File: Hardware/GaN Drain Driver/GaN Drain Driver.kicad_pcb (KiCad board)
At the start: 4 copper layers, 101.6 x 50.8 mm, 64 parts, among them J1 SMA-J-P-H-ST-EM1, J2 Conn_01x02_Socket, J3 Conn_01x02_Socket, J4 Conn_01x02_Socket, Q1 NVD360N65S3T4G, Q2 NVD360N65S3T4G, U1 IRS2008S, U2 LM393, U3 L7815, U4 R1SE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

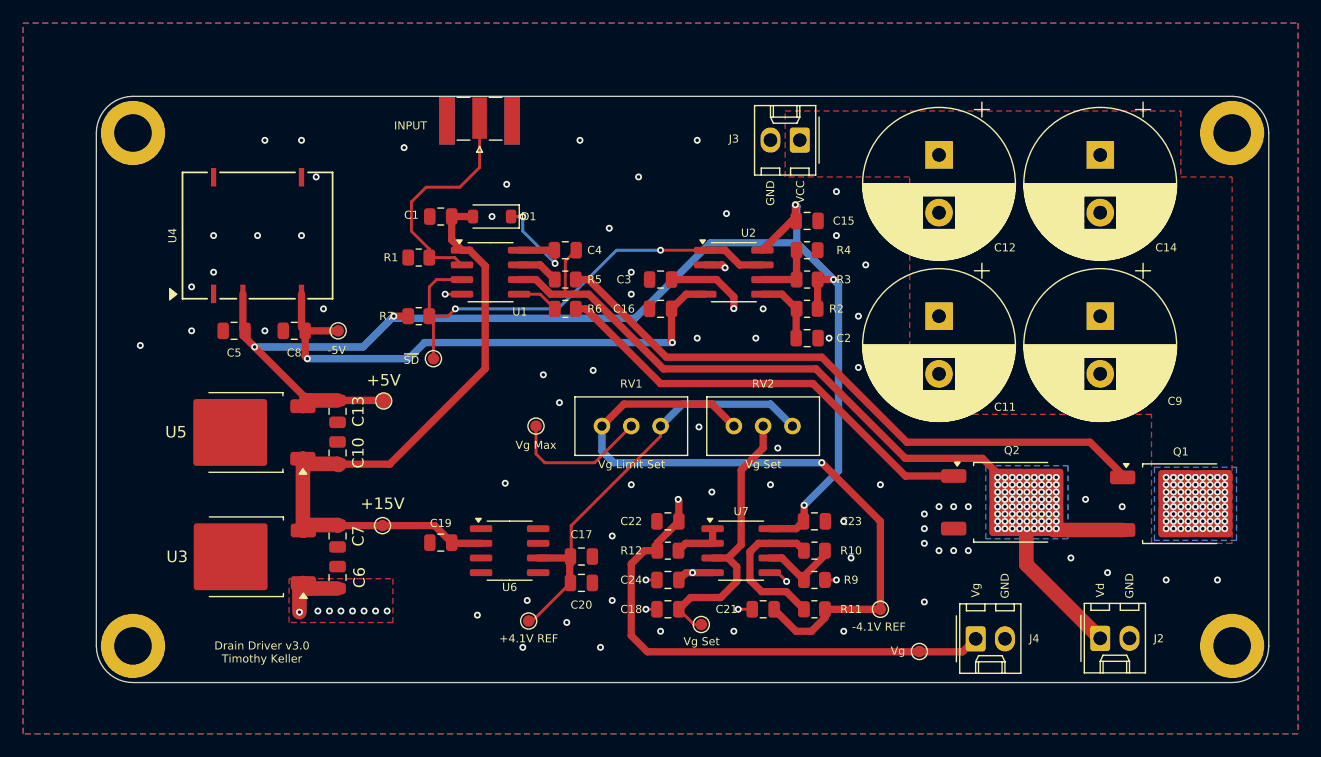
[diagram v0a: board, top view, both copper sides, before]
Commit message: Adding BOM, Fixing schematic issue
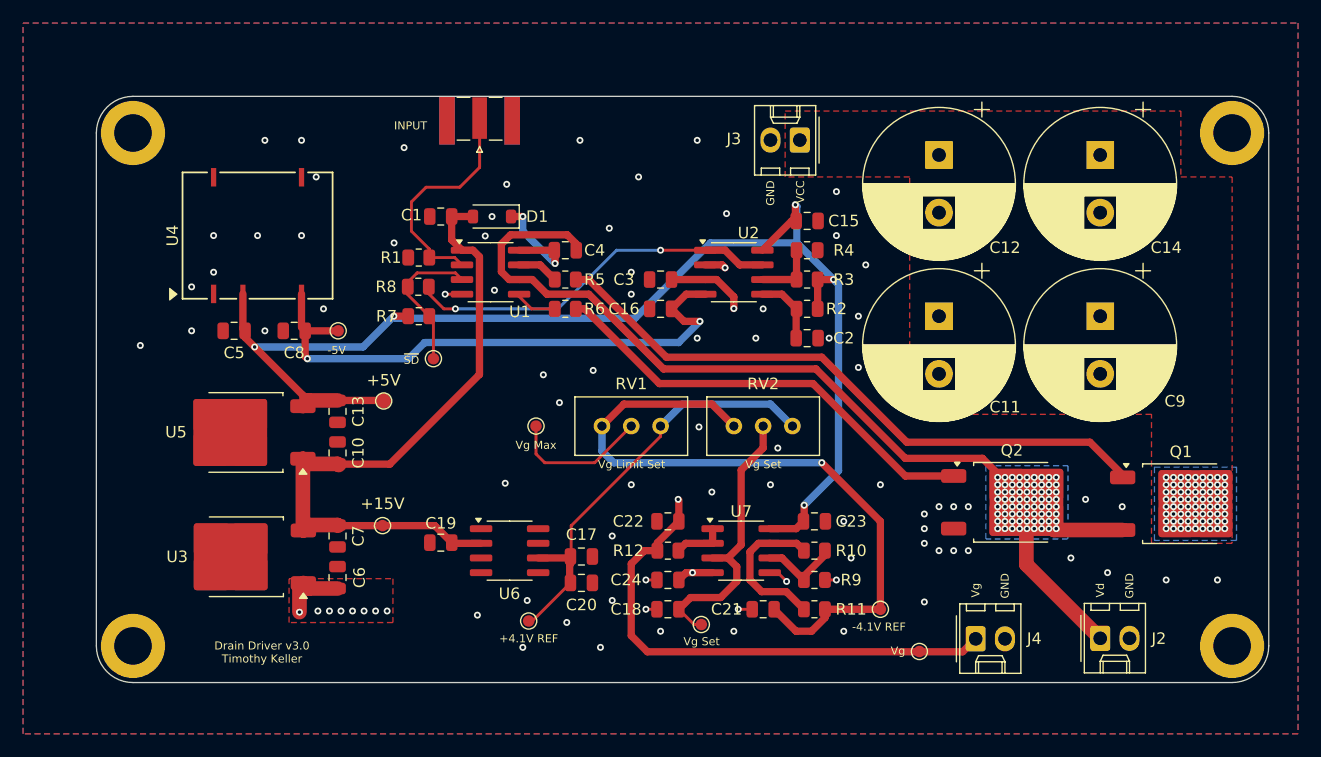
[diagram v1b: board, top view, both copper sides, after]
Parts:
- added R8: 10k, Resistor_SMD:R_0805_2012Metric, F.Cu at (78.7, 41.9)
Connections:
- R7 pad 2: COMP_OUT -> ~{SD}
- TP2 pad 1: COMP_OUT -> ~{SD}
- U1 pad 3: COMP_OUT -> ~{SD}
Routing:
- net ~{SD}: track 0.00 -> 12.8 mm
- net COMP_OUT: track 41.2 -> 32.7 mm
- net Vd: track 80.5 -> 88.2 mm
- net -5V: track 91.5 -> 94.6 mm
- net GND: vias 74 -> 77

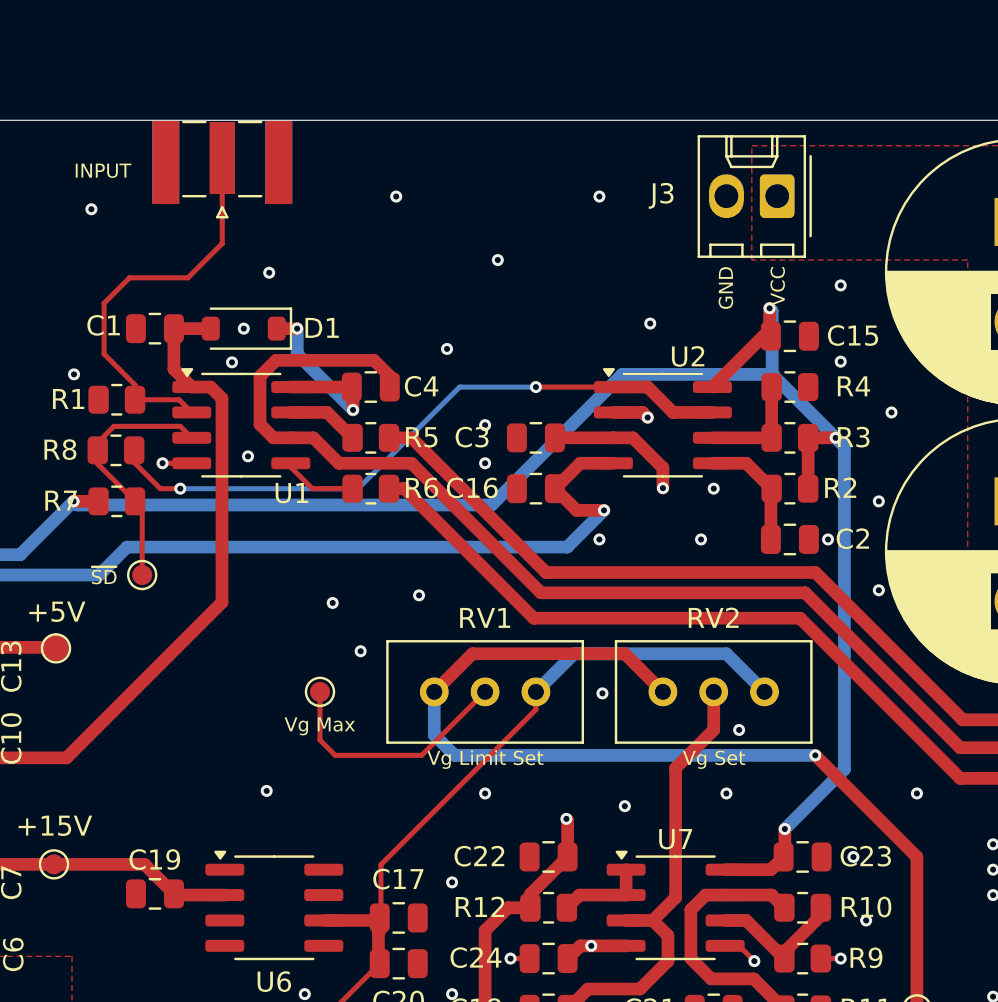
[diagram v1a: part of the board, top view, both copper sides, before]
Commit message: Updating SMA footprint
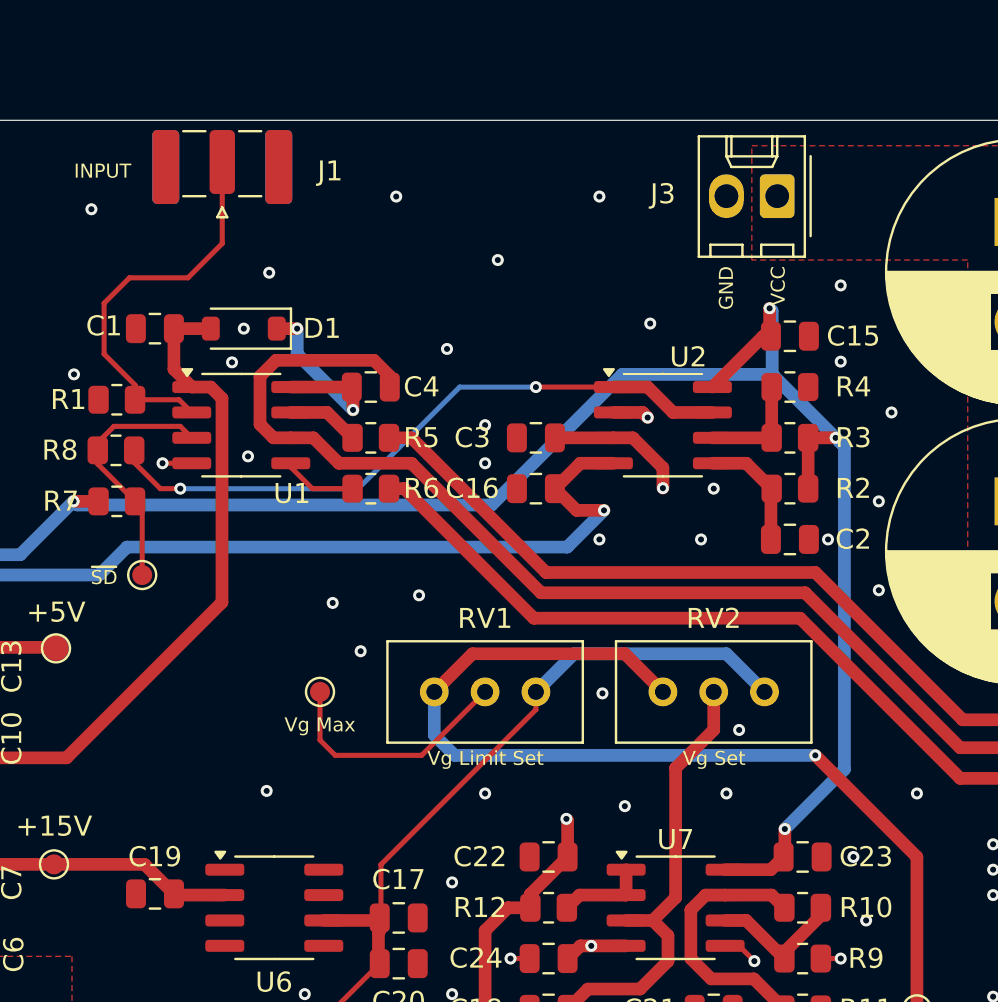
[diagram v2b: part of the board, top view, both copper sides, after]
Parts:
- J1: footprint Connector_Coaxial:SMA_Samtec_SMA-J-P-X-ST-EM1_EdgeMount -> Connector_Coaxial:SMA_Samtec_SMA-J-P-H-ST-EM1_EdgeMount
- turned J1 to 90 degrees
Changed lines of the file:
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@@
 			(psa4output no)
 			(plot_black_and_white yes)
-			(plotinvisibletext no)
 			(sketchpadsonfab no)
 			(plotpadnumbers no)
@@
 		(tags "resistor")
 		(property "Reference" "R2"
-			(at -2.54 0 180)
+			(at -3.175 0 180)
 			(layer "F.SilkS")
 			(effects
@@
 		)
 	)
-	(footprint "Connector_Coaxial:SMA_Samtec_SMA-J-P-X-ST-EM1_EdgeMount"
+	(footprint "Connector_Coaxial:SMA_Samtec_SMA-J-P-H-ST-EM1_EdgeMount"
 		(layer "F.Cu")
-		(at 84.012 27.4828 180)
+		(at 84.012 27.4828 90)
 		(descr "Connector SMA, 0Hz to 20GHz, 50Ohm, Edge Mount (http://suddendocs.samtec.com/prints/sma-j-p-x-st-em1-mkt.pdf)")
 		(tags "SMA Straight Samtec Edge Mount")
 		(property "Reference" "J1"
-			(at 0 -3.5 180)
+			(at -0.4572 5.396 180)
 			(layer "F.SilkS")
-			(hide yes)
 			(effects
 				(font
@@
 		)
 		(property "Value" "SMA-J-P-H-ST-EM1"
-			(at 0 13 180)
+			(at 0 7.62 90)
 			(layer "F.Fab")
 			(hide yes)
@@
 		)
 		(property "Digikey" "SAM8857-ND"
-			(at 0 0 180)
+			(at 0 0 90)
 			(unlocked yes)
 			(layer "F.Fab")
@@
 		)
 		(property "Sim.Pin" ""
-			(at 0 0 180)
+			(at 0 0 90)
 			(unlocked yes)
 			(layer "F.Fab")
@@
 		)
 		(property "MPN" "SMA-J-P-H-ST-EM1"
-			(at 0 0 180)
+			(at 0 0 90)
 			(unlocked yes)
 			(layer "F.Fab")
@@
 		)
 		(property "Manufacturer" "Samtec Inc."
-			(at 0 0 180)
+			(at 0 0 90)
 			(unlocked yes)
 			(layer "F.Fab")
@@
 		(attr smd)
 		(fp_line
-			(start 0.84 2)
-			(end 1.95 2)
+			(start 1.54 -0.84)
+			(end 1.54 -1.95)
 			(stroke
 				(width 0.12)
@@
 		)
 		(fp_line
-			(start 0.84 -1.71)
-			(end 1.95 -1.71)
+			(start -1.71 -0.84)
+			(end -1.71 -1.95)
 			(stroke
 				(width 0.12)
@@
 		)
 		(fp_line
-			(start 0.25 -2.76)
-			(end -0.25 -2.76)
+			(start -2.76 -0.25)
+			(end -2.76 0.25)
 			(stroke
 				(width 0.12)
@@
 		)
 		(fp_line
-			(start 0 -2.26)
-			(end 0.25 -2.76)
+			(start -2.26 0)
+			(end -2.76 -0.25)
 			(stroke
 				(width 0.12)
@@
 		)
 		(fp_line
-			(start -0.25 -2.76)
-			(end 0 -2.26)
+			(start -2.76 0.25)
+			(end -2.26 0)
 			(stroke
 				(width 0.12)
@@
 		)
 		(fp_line
-			(start -1.95 2)
-			(end -0.84 2)
+			(start 1.54 1.95)
+			(end 1.54 0.84)
 			(stroke
 				(width 0.12)
@@
 		)
 		(fp_line
-			(start -1.95 -1.71)
-			(end -0.84 -1.71)
+			(start -1.71 1.95)
+			(end -1.71 0.84)
 			(stroke
 				(width 0.12)
@@
 		)
 		(fp_line
-			(start 4.1 2.1)
-			(end -4.1 2.1)
+			(start 2.1 -4.1)
+			(end 2.1 4.1)
 			(stroke
 				(width 0.1)
@@
 		)
 		(fp_line
-			(start 4 2.6)
-			(end 4 -2.6)
+			(start 2.6 -4)
+			(end -2.6 -4)
 			(stroke
 				(width 0.05)
@@
 		)
 		(fp_line
-			(start 4 2.6)
-			(end 3.68 2.6)
+			(start 2.6 -4)
+			(end 2.6 -3.68)
 			(stroke
 				(width 0.05)
@@
 		)
 		(fp_line
-			(start 3.68 12.12)
-			(end -3.68 12.12)
+			(start 12.12 -3.68)
+			(end 12.12 3.68)
 			(stroke
 				(width 0.05)
@@
 		)
 		(fp_line
-			(start 3.68 2.6)
-			(end 3.68 12.12)
+			(start 2.6 -3.68)
+			(end 12.12 -3.68)
 			(stroke
 				(width 0.05)
@@
 		)
 		(fp_line
-			(start -3.68 12.12)
-			(end -3.68 2.6)
+			(start 12.12 3.68)
+			(end 2.6 3.68)
 			(stroke
 				(width 0.05)
@@
 		)
 		(fp_line
-			(start -3.68 2.6)
-			(end -4 2.6)
+			(start 2.6 3.68)
+			(end 2.6 4)
 			(stroke
 				(width 0.05)
@@
 		)
 		(fp_line
-			(start -4 2.6)
-			(end -4 -2.6)
+			(start 2.6 4)
+			(end -2.6 4)
 			(stroke
 				(width 0.05)
@@
 		)
 		(fp_line
-			(start -4 -2.6)
-			(end 4 -2.6)
+			(start -2.6 4)
+			(end -2.6 -4)
 			(stroke
 				(width 0.05)
@@
 		)
 		(fp_line
-			(start 4 2.6)
-			(end 4 -2.6)
+			(start 2.6 -4)
+			(end -2.6 -4)
 			(stroke
 				(width 0.05)
@@
 		)
 		(fp_line
-			(start 3.68 12.12)
-			(end -3.68 12.12)
+			(start 12.12 -3.68)
+			(end 12.12 3.68)
 			(stroke
 				(width 0.05)
@@
 		)
 		(fp_line
-			(start 3.68 2.6)
-			(end 4 2.6)
+			(start 2.6 -3.68)
+			(end 2.6 -4)
 			(stroke
 				(width 0.05)
@@
 		)
 		(fp_line
-			(start 3.68 2.6)
-			(end 3.68 12.12)
+			(start 2.6 -3.68)
+			(end 12.12 -3.68)
 			(stroke
 				(width 0.05)
@@
 		)
 		(fp_line
-			(start -3.68 12.12)
-			(end -3.68 2.6)
+			(start 12.12 3.68)
+			(end 2.6 3.68)
 			(stroke
 				(width 0.05)
@@
 		)
 		(fp_line
-			(start -3.68 2.6)
-			(end -4 2.6)
+			(start 2.6 3.68)
+			(end 2.6 4)
 			(stroke
 				(width 0.05)
@@
 		)
 		(fp_line
-			(start -4 2.6)
-			(end -4 -2.6)
+			(start 2.6 4)
+			(end -2.6 4)
 			(stroke
 				(width 0.05)
@@
 		)
 		(fp_line
-			(start -4 -2.6)
-			(end 4 -2.6)
+			(start -2.6 4)
+			(end -2.6 -4)
 			(stroke
 				(width 0.05)
@@
 		)
 		(fp_line
-			(start 3.175 -1.71)
-			(end 3.175 11.62)
+			(start -1.71 -3.175)
+			(end 11.62 -3.175)
 			(stroke
 				(width 0.1)
@@
 		)
 		(fp_line
-			(start 3.175 -1.71)
-			(end 2.365 -1.71)
+			(start -1.71 -3.175)
+			(end -1.71 -2.365)
 			(stroke
 				(width 0.1)
@@
 		)
 		(fp_line
-			(start 3.165 11.62)
-			(end -3.165 11.62)
+			(start 11.62 -3.165)
+			(end 11.62 3.165)
 			(stroke
 				(width 0.1)
@@
 		)
 		(fp_line
-			(start 2.365 2.1)
-			(end -2.365 2.1)
+			(start 2.1 -2.365)
+			(end 2.1 2.365)
 			(stroke
 				(width 0.1)
@@
 		)
 		(fp_line
-			(start 2.365 -1.71)
-			(end 2.365 2.1)
+			(start -1.71 -2.365)
+			(end 2.1 -2.365)
 			(stroke
 				(width 0.1)
@@
 		)
 		(fp_line
-			(start 0.64 2.1)
-			(end 0 3.1)
+			(start 2.1 -0.64)
+			(end 3.1 0)
 			(stroke
 				(width 0.1)
@@
 		)
 		(fp_line
-			(start 0 3.1)
-			(end -0.64 2.1)
+			(start 3.1 0)
+			(end 2.1 0.64)
 			(stroke
 				(width 0.1)
@@
 		)
 		(fp_line
-			(start -2.365 2.1)
-			(end -2.365 -1.71)
+			(start 2.1 2.365)
+			(end -1.71 2.365)
 			(stroke
 				(width 0.1)
@@
 		)
 		(fp_line
-			(start -2.365 -1.71)
-			(end -3.175 -1.71)
+			(start -1.71 2.365)
+			(end -1.71 3.175)
 			(stroke
 				(width 0.1)
@@
 		)
 		(fp_line
-			(start -3.175 -1.71)
-			(end -3.175 11.62)
+			(start -1.71 3.175)
+			(end 11.62 3.175)
 			(stroke
 				(width 0.1)
@@
 		)
 		(fp_text user "PCB Edge"
-			(at 0 2.6 180)
+			(at 2.6 0 0)
 			(layer "Dwgs.User")
 			(effects
@@
 		)
 		(fp_text user "${REFERENCE}"
-			(at 0 4.79 180)
+			(at 0 0 90)
 			(layer "F.Fab")
 			(effects
@@
 			)
 		)
-		(pad "1" smd rect
-			(at 0 0.2 180)
-			(size 1.27 3.6)
-			(layers "F.Cu" "F.Mask" "F.Paste")
+		(pad "1" smd roundrect
+			(at 0 0 180)
+			(size 1.27 3.2)
+			(layers "F.Cu" "F.Mask")
+			(roundrect_rratio 0.1968503937)
 			(net 4 "Net-(J1-In)")
 			(pinfunction "In")
 			(pintype "passive")
 		)
-		(pad "2" smd rect
-			(at -2.825 0 180)
-			(size 1.35 4.2)
-			(layers "F.Cu" "F.Mask" "F.Paste")
+		(pad "2" smd roundrect
+			(at -0.25 -2.825 180)
+			(size 1.35 3.7)
+			(layers "F.Cu" "F.Mask")
+			(roundrect_rratio 0.1851851852)
 			(net 2 "GND")
 			(pinfunction "Ext")
 			(pintype "passive")
 		)
-		(pad "2" smd rect
-			(at -2.825 0 180)
-			(size 1.35 4.2)
-			(layers "B.Cu" "B.Mask" "B.Paste")
+		(pad "2" smd roundrect
+			(at -0.25 -2.825 180)
+			(size 1.35 3.7)
+			(layers "B.Cu" "B.Mask")
+			(roundrect_rratio 0.1851851852)
 			(net 2 "GND")
 			(pinfunction "Ext")
 			(pintype "passive")
 		)
-		(pad "2" smd rect
-			(at 2.825 0 180)
-			(size 1.35 4.2)
-			(layers "F.Cu" "F.Mask" "F.Paste")
+		(pad "2" smd roundrect
+			(at -0.25 2.825 180)
+			(size 1.35 3.7)
+			(layers "F.Cu" "F.Mask")
+			(roundrect_rratio 0.1851851852)
 			(net 2 "GND")
 			(pinfunction "Ext")
 			(pintype "passive")
 		)
-		(pad "2" smd rect
-			(at 2.825 0 180)
-			(size 1.35 4.2)
-			(layers "B.Cu" "B.Mask" "B.Paste")
+		(pad "2" smd roundrect
+			(at -0.25 2.825 180)
+			(size 1.35 3.7)
+			(layers "B.Cu" "B.Mask")
+			(roundrect_rratio 0.1851851852)
 			(net 2 "GND")
 			(pinfunction "Ext")
@@
 		)
 		(embedded_fonts no)
-		(model "${KICAD8_3DMODEL_DIR}/Connector_Coaxial.3dshapes/SMA_Samtec_SMA-J-P-X-ST-EM1_EdgeMount.wrl"
+		(model "${KICAD9_3DMODEL_DIR}/Connector_Coaxial.3dshapes/SMA_Samtec_SMA-J-P-H-ST-EM1_EdgeMount.step"
 			(offset
 				(xyz 0 0 0)
@@
 		(tags "capacitor")
 		(property "Reference" "C19"
-			(at 0 -1.68 0)
+			(at 0 -1.845 0)
 			(layer "F.SilkS")
 			(effects

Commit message: Running DRC on PCB
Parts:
- J2, J3, J4: value Conn_01x02_Socket -> 0022272021
- moved H4 0.18 mm to (54.1, 72.9)
- moved H2 0.18 mm to (54.1, 28.7)
- moved H3 0.18 mm to (149.1, 72.9)
- moved H1 0.18 mm to (149.1, 28.7)
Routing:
- net Vg: track 73.1 -> 77.3 mm
- net GND: vias 77 -> 78
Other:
- outline, holes or cut-outs redrawn
